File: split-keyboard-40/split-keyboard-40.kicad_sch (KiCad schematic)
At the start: 85 parts, among them SW1 Switch, SW10 Switch, SW11 Switch, SW12 Switch, SW13 Switch, SW14 Switch, SW15 Switch, SW16 Switch, SW17 Switch, SW18 Switch, SW19 Switch, SW2 Switch, SW20 Switch, SW21 Switch, SW22 Switch, SW23 Switch, SW24 Switch, SW25 Switch, SW26 Switch, SW27 Switch, SW28 Switch, SW29 Switch, SW3 Switch, SW30 Switch, SW31 Switch, SW32 Switch, SW33 Switch, SW34 Switch, SW35 Switch, SW36 Switch, SW37 Switch, SW38 Switch, SW39 Switch, SW4 Switch, SW40 Switch, SW41 Switch, SW42 Switch, SW5 Switch, SW6 Switch, SW7 Switch, SW8 Switch, SW9 Switch, U1 Raspberry_Pi_Pico

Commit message: few rows
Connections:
- net col_1: now also U1.7 (GPIO5); no longer U1.5 (GPIO3)
- net col_10: now also U1.25 (GPIO19); no longer U1.16 (GPIO12)
- net col_11: now also U1.24 (GPIO18); no longer U1.17 (GPIO13)
- net col_12: now also U1.22 (GPIO17); no longer U1.19 (GPIO14)
- net col_3: now also U1.5 (GPIO3); no longer U1.7 (GPIO5)
- net col_4: now also U1.4 (GPIO2); no longer U1.9 (GPIO6)
- net col_5: now also U1.2 (GPIO1); no longer U1.10 (GPIO7)
- net col_6: now also U1.1 (GPIO0); no longer U1.11 (GPIO8)
- net col_7: now also U1.29 (GPIO22); no longer U1.12 (GPIO9)
- net col_8: now also U1.27 (GPIO21); no longer U1.14 (GPIO10)
- net col_9: now also U1.26 (GPIO20); no longer U1.15 (GPIO11)
- net row_1: now also U1.9 (GPIO6); no longer U1.1 (GPIO0)
- net row_2: now also U1.10 (GPIO7); no longer U1.2 (GPIO1)
- net row_3: now also U1.11 (GPIO8); no longer U1.4 (GPIO2)

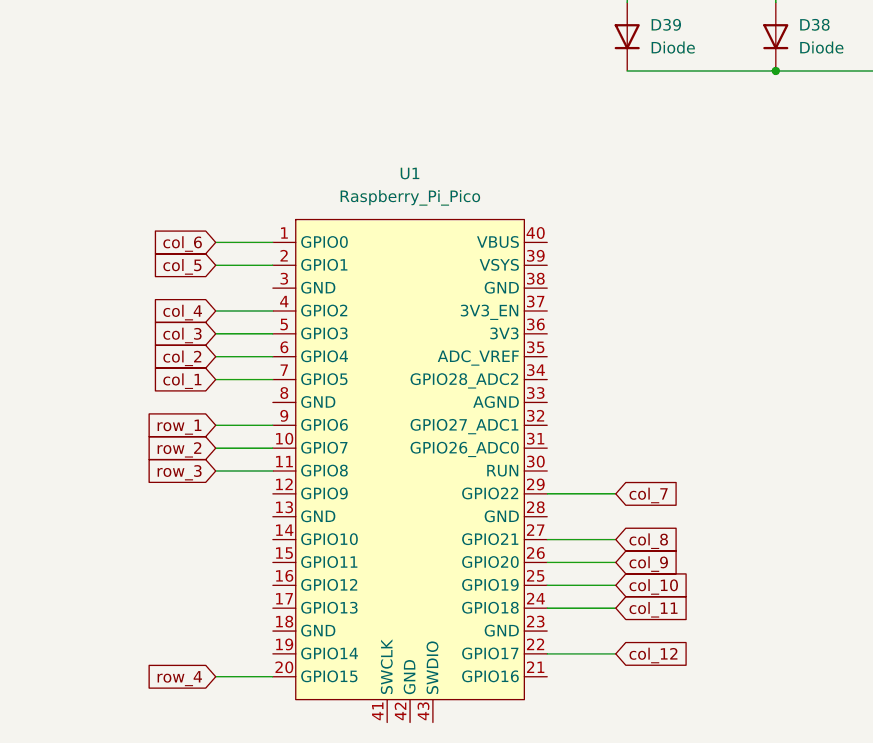
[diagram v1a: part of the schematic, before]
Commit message: ergogen layout + elite-c
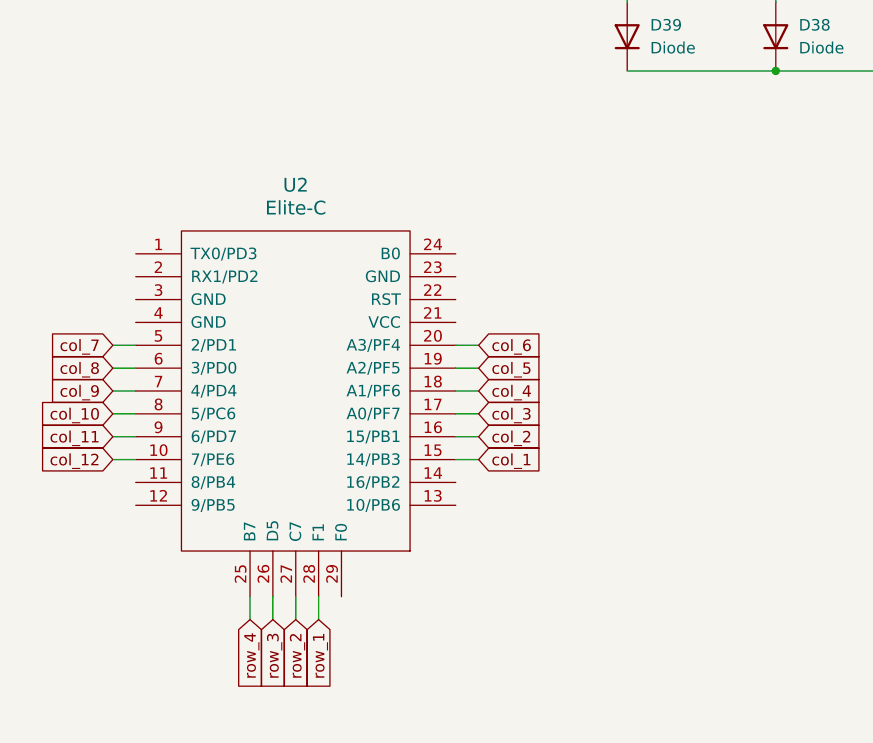
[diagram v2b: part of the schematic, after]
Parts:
- removed U1: Raspberry_Pi_Pico, ScottoKeebs_MCU:Raspberry_Pi_Pico, symbol Keboards:MCU_Raspberry_Pi_Pico
- added U2: Elite-C, Keebio-Parts:Elite-C, symbol keebio:Elite-C
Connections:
- net col_1: now also U2.15 (14/PB3)
- net col_10: now also U2.8 (5/PC6)
- net col_11: now also U2.9 (6/PD7)
- net col_12: now also U2.10 (7/PE6)
- net col_2: now also U2.16 (15/PB1)
- net col_3: now also U2.17 (A0/PF7)
- net col_4: now also U2.18 (A1/PF6)
- net col_5: now also U2.19 (A2/PF5)
- net col_6: now also U2.20 (A3/PF4)
- net col_7: now also U2.5 (2/PD1)
- net col_8: now also U2.6 (3/PD0)
- net col_9: now also U2.7 (4/PD4)
- net row_1: now also U2.28 (F1)
- net row_2: now also U2.27 (C7)
- net row_3: now also U2.26 (D5)
- net row_4: now also U2.25 (B7)
